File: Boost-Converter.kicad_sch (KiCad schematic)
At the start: 6 parts

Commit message: WIP boost converter
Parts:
- added C?: (no value), symbol Device:C
- added C?: 100n, symbol Device:C
- added R?: 110k, symbol Device:R
- added R?: 220k, symbol Device:R
- C? (x4): value ~ -> 22u 70V
- C?: value (none) -> 180u 70V; symbol Device:C -> Device:C_Polarized
- U?: value (none) -> LTC3769-QFN; footprint (none) -> Package_DFN_QFN:WQFN-24-1EP_4x4mm_P0.5mm_EP2.45x2.45mm_ThermalVias
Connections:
- net VIN: now reaches C?.1
- net VIN: now also C?.1, C?.1, C?.1, C?.1, R?.1
- net GND: now reaches C?.2
- net GND: now also C?.2, C?.2, C?.2, C?.2, U?.10 (GND), U?.24 (GND), U?.25 (GND), U?.8 (GND), C?.2, C?.2, R?.2
- net at U?.11 (RUN): now also R?.2
- net SS: now reaches U?.12 (SS)
- net SS: now also C?.1
- net ITH: now reaches U?.16 (ITH)
- net INTV_{CC}: now reaches U?.22 (INTV_{CC}), U?.5 (INTV_{CC})
- net INTV_{CC}: now also U?.9 (PLLIN/MODE), C?.1
- net at U?.7 (FREQ): now also R?.1
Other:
- note added: "Frequency is set to ~900kHz"
- note added: "RUN pin cannot be tied to the input voltage, but through resistor it's allowed (must not exceeding 100µA)"
- note added: "input capacity"
- moved on the sheet: C?, U?

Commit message: Finish boost converter
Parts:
- removed C? (x3): 22u 70V, symbol Device:C
- removed C?: 180u 70V, symbol Device:C_Polarized
- added C? (x4): 22u 70V, symbol Device:C
- added C?: 180u 70V, symbol Device:C_Polarized
- added C? (x2): (no value), symbol Device:C
- added D?: (no value), symbol Device:D_Schottky
- added L?: (no value), symbol Device:L
- added Q? (x2): (no value), symbol extraSymbols:BSC016N06NS
- added R? (x3): (no value), symbol Device:R
- added R?: (no value), symbol Device:R_Shunt
- C?: value 22u 70V -> (none)
- C?: value (none) -> 10u
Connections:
- net VIN is gone; now on net V_{IN}: C?.1, R?.1
- net GND: now also U?.23 (EXTV~{CC}), U?.3 (ILIM), C?.2, C?.2, C?.2, C?.2, C?.2, Q?.1 (S), Q?.2 (S), Q?.3 (S), R?.1
- net INTV_{CC}: now also U?.17 (OVMODE), D?.2 (A), R?.1
- net V_{IN}: now reaches U?.1 (VBIAS)
- net V_{IN}: now also R?.1
- net at U?.13 (Sense-): now also C?.2, R?.3
- net at U?.14 (Sense+): now also C?.1, R?.2
- net at U?.15 (VFB): now also R?.1, R?.2
- net at U?.18 (SW): now also C?.1, L?.2, Q?.1 (S), Q?.2 (S), Q?.3 (S), Q?.5 (D)
- net at U?.19 (TG): now also Q?.4 (G)
- net at U?.2 (PGOOD): now also R?.2
- net at U?.20 (BOOST): now also C?.2, D?.1 (K)
- net at U?.21 (BG): now also Q?.4 (G)
- new net: L?.1, R?.4
- new net V_{OUT}: C?.1, C?.1, C?.1, C?.1, C?.1, Q?.5 (D), R?.2
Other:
- note added: "I_{maxIn} = 5A @100W I_{rippleDelta} = 0.3 * I_{maxIn} = 1.5A L = (20V / (900kHz * 1.5A)) * (1 - (20V / 50,4V)) L = 8.936uH -> 8.2uH R_{Sense} = 50mV / (I_{maxIn} + (I_{rippleDelta} / 2)) R_{Sense} = 8mOhm -> we use 5mOhm"
- note added: "output capacity"
- note added: "set to 50mV"
- note added: "set voltage divider to 55.6V V_{Out}"
- moved on the sheet: C?

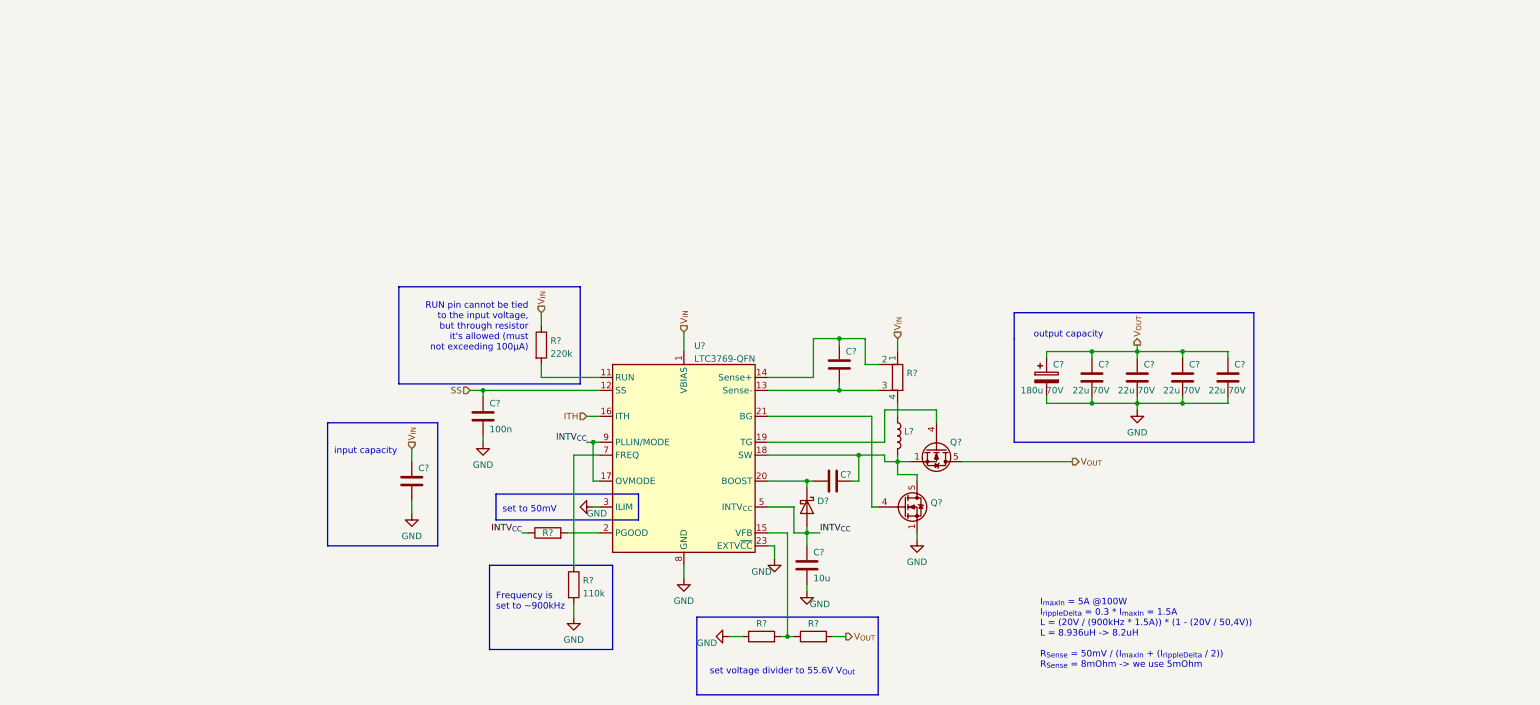
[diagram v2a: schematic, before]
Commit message: Finish schematic
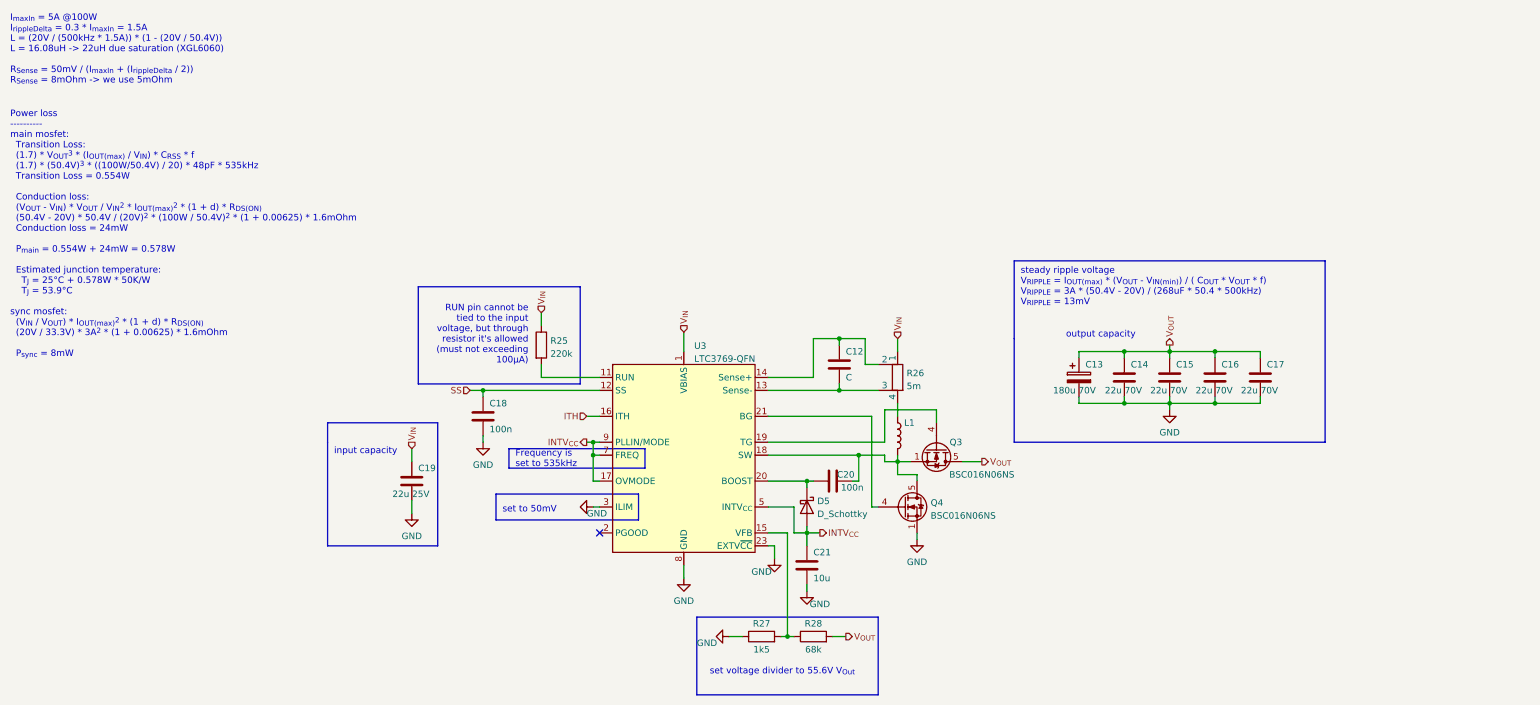
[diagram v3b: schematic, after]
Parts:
- removed R?: (no value), symbol Device:R
- removed R?: 110k, symbol Device:R
- C12: renamed from C?; value (none) -> C
- C19: renamed from C?; value (none) -> 22u 25V
- C20: renamed from C?; value (none) -> 100n
- D5: renamed from D?; value (none) -> D_Schottky
- Q3, Q4: renamed from Q?; value (none) -> BSC016N06NS; footprint (none) -> Package_TO_SOT_SMD:TDSON-8-1
- R26: renamed from R?; value (none) -> 5m
- R27: renamed from R?; value (none) -> 1k5
- R28: renamed from R?; value (none) -> 68k
- gave numbers to parts that had none: 10
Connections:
- net INTV_{CC}: now also U3.7 (FREQ)
- net at U3.4 (NC): no longer U3.6 (NC)
- no-connect marks 0 -> 1
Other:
- note added: "Frequency is set to 535kHz"
- note added: "I_{maxIn} = 5A @100W I_{rippleDelta} = 0.3 * I_{maxIn} = 1.5A L = (20V / (500kHz * 1.5A)) * (1 - (20V / 50.4V)) L = 16.08uH -> 22uH due saturation (XGL6060) R_{Sense} = 50mV / (I_{maxIn} + (I_{rippleDelta} / 2)) R_{Sense} = 8mOhm -> we use 5mOhm"
- note added: "Power loss ---------- main mosfet: Transition Loss: (1.7) * V_{OUT}^{3} * (I_{OUT(max)} / V_{IN}) * C_{RSS} * f (1.7) * (50.4V)^{3} * ((100W/50.4V) / 20) * 48pF * 535kHz Transition Loss = 0.554W Conduction loss: (V_{OUT} - V_{IN}) * V_{OUT} / V_{IN}^{2} * I_{OUT(max)}^{2} * (1 + d) * R_{DS(ON)} (50.4V - 20V) * 50.4V / (20V)^{2} * (100W / 50.4V)^{2} * (1 + 0.00625) * 1.6mOhm Conduction loss = 24mW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"
- note added: "steady ripple voltage V_{RIPPLE} = I_{OUT(max)} * (V_{OUT} - V_{IN(min)}) / ( C_{OUT} * V_{OUT} * f) V_{RIPPLE} = 3A * (50.4V - 20V) / (268uF * 50.4 * 500kHz) V_{RIPPLE} = 13mV"
- note removed: "Frequency is set to ~900kHz"
- note removed: "I_{maxIn} = 5A @100W I_{rippleDelta} = 0.3 * I_{maxIn} = 1.5A L = (20V / (900kHz * 1.5A)) * (1 - (20V / 50,4V)) L = 8.936uH -> 8.2uH R_{Sense} = 50mV / (I_{maxIn} + (I_{rippleDelta} / 2)) R_{Sense} = 8mOhm -> we use 5mOhm"
- moved on the sheet: C13, C14, C15, C16, C17

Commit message: Small changes
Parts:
- added C? (x3): 22u 25V, Capacitor_SMD:C_0805_2012Metric, symbol Device:C
- C12, C18, C20: footprint (none) -> Capacitor_SMD:C_0603_1608Metric
- C13: footprint (none) -> Capacitor_THT:CP_Radial_D8.0mm_P2.50mm
- C19, C21: footprint (none) -> Capacitor_SMD:C_0805_2012Metric
- L1: value (none) -> XGL6060-223; footprint (none) -> Inductor_SMD:L_Coilcraft_XAL60xx_6.36x6.56mm
- R25, R27, R28: footprint (none) -> Resistor_SMD:R_0603_1608Metric
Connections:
- net GND: now also C?.2, C?.2, C?.2
- net V_{IN}: now also C?.1, C?.1, C?.1
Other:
- moved on the sheet: C19

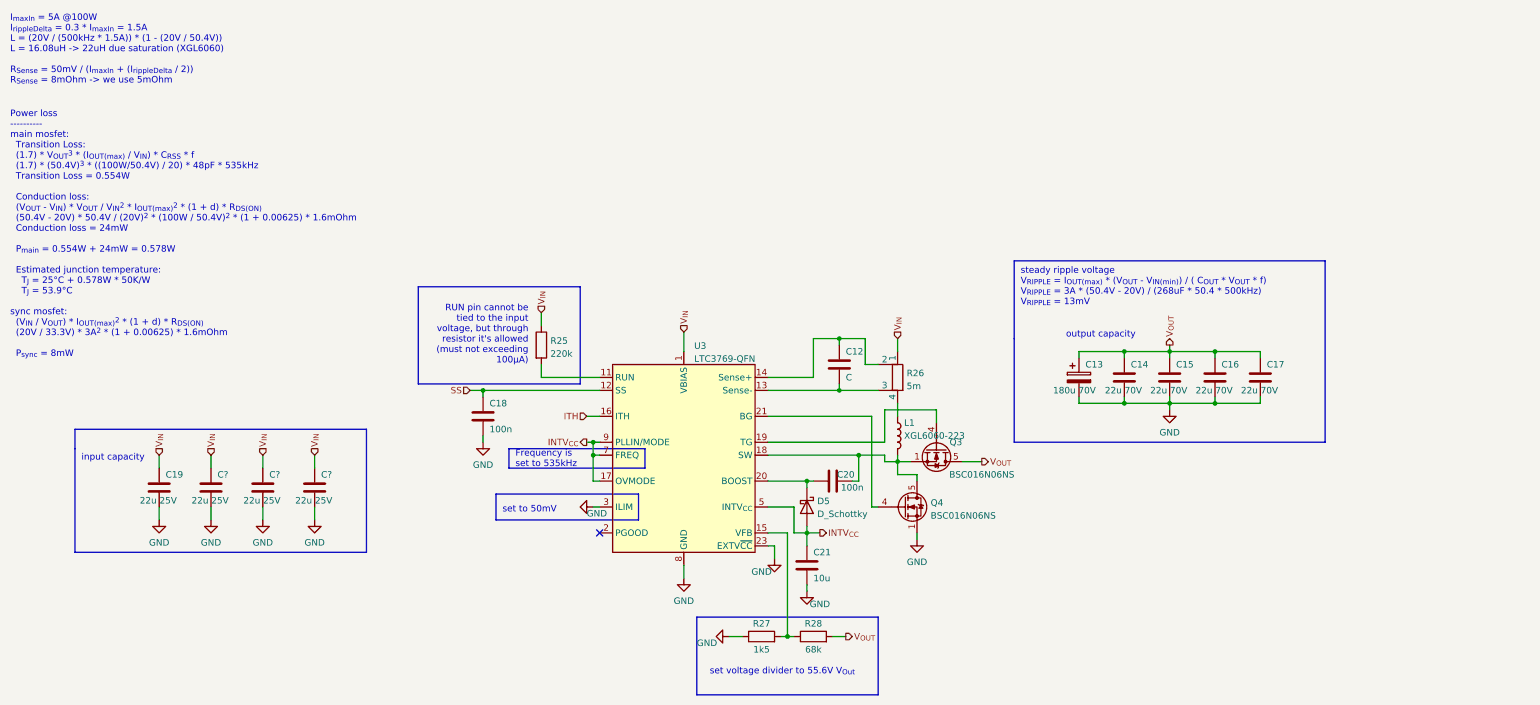
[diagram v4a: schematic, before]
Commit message: Annotate symbols and assign footprints
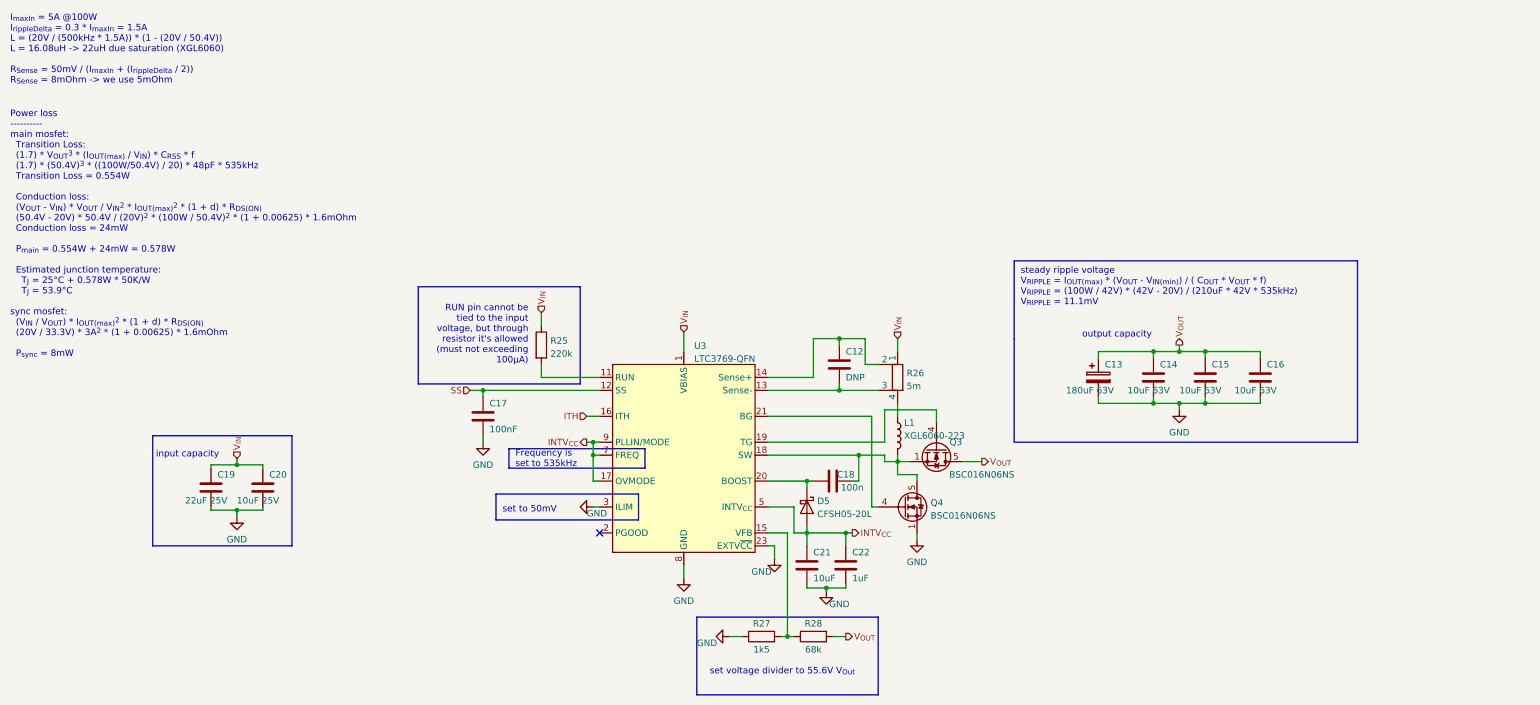
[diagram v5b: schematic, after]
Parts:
- removed C17: 22u 70V, symbol Device:C
- removed C19, C?: 22u 25V, Capacitor_SMD:C_0805_2012Metric, symbol Device:C
- added C22: 1uF, Capacitor_SMD:C_0805_2012Metric, symbol Device:C
- C12: value C -> DNP
- C13: value 180u 70V -> 180uF 63V; footprint Capacitor_THT:CP_Radial_D8.0mm_P2.50mm -> Capacitor_THT:CP_Radial_D10.0mm_P5.00mm
- C14, C15, C16: value 22u 70V -> 10uF 63V; footprint (none) -> Capacitor_SMD:C_1210_3225Metric
- C17: renamed from C18; value 100n -> 100nF
- C19: renamed from C?; value 22u 25V -> 22uF 25V
- C20: renamed from C?; value 22u 25V -> 10uF 25V
- C21: value 10u -> 10uF
- D5: value D_Schottky -> CFSH05-20L; footprint (none) -> extraFootprints:SOD882D
- R26: footprint (none) -> extraFootprints:R_1206_3216Metric_4Kelvin
- renumbered C20 to C18
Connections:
- net GND: now also C22.2
- net INTV_{CC}: now also C22.1
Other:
- note added: "steady ripple voltage V_{RIPPLE} = I_{OUT(max)} * (V_{OUT} - V_{IN(min)}) / ( C_{OUT} * V_{OUT} * f) V_{RIPPLE} = (100W / 42V) * (42V - 20V) / (210uF * 42V * 535kHz) V_{RIPPLE} = 11.1mV"
- note removed: "steady ripple voltage V_{RIPPLE} = I_{OUT(max)} * (V_{OUT} - V_{IN(min)}) / ( C_{OUT} * V_{OUT} * f) V_{RIPPLE} = 3A * (50.4V - 20V) / (268uF * 50.4 * 500kHz) V_{RIPPLE} = 13mV"
- moved on the sheet: C13, C14, C15, C16

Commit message: Update BOM due component order
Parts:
- C22: footprint Capacitor_SMD:C_0805_2012Metric -> Capacitor_SMD:C_0603_1608Metric
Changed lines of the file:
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@@
       (effects (font (size 1.27 1.27)) (justify left))
     )
-    (property "Footprint" "Capacitor_SMD:C_0805_2012Metric" (id 2) (at 178.7652 125.73 0)
+    (property "Footprint" "Capacitor_SMD:C_0603_1608Metric" (id 2) (at 178.7652 125.73 0)
       (effects (font (size 1.27 1.27)) hide)
     )

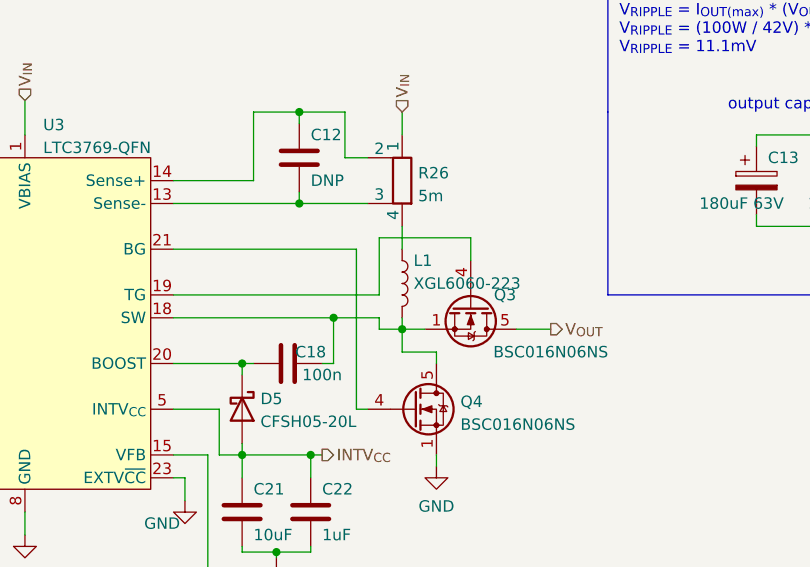
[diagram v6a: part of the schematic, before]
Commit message: Update to KiCad 7
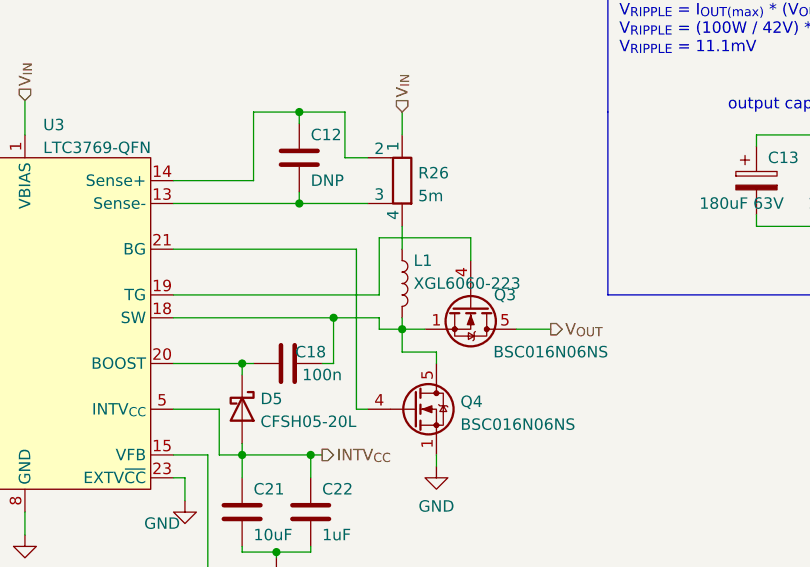
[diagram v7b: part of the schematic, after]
